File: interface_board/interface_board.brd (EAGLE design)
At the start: 65 x 56 mm, 91 parts, among them IC1 V7805-1000, IC6 LAN9512-JZX, K2 61400826021, Q1 IRLML6346TRPBF, Q6 FA-238 25.0000MB, U1 AL5812MP-13, U2 MPU-9250

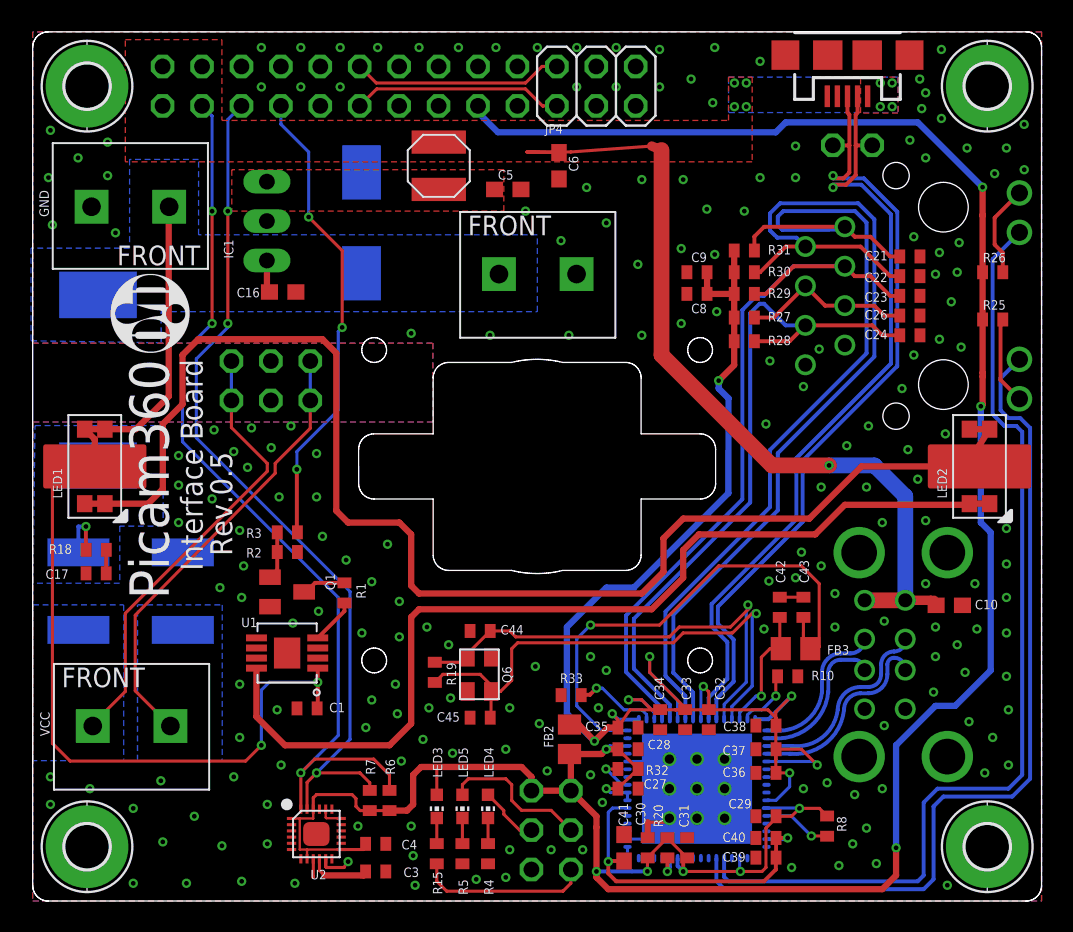
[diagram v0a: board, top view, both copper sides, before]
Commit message: camera_unit, camera_adapter
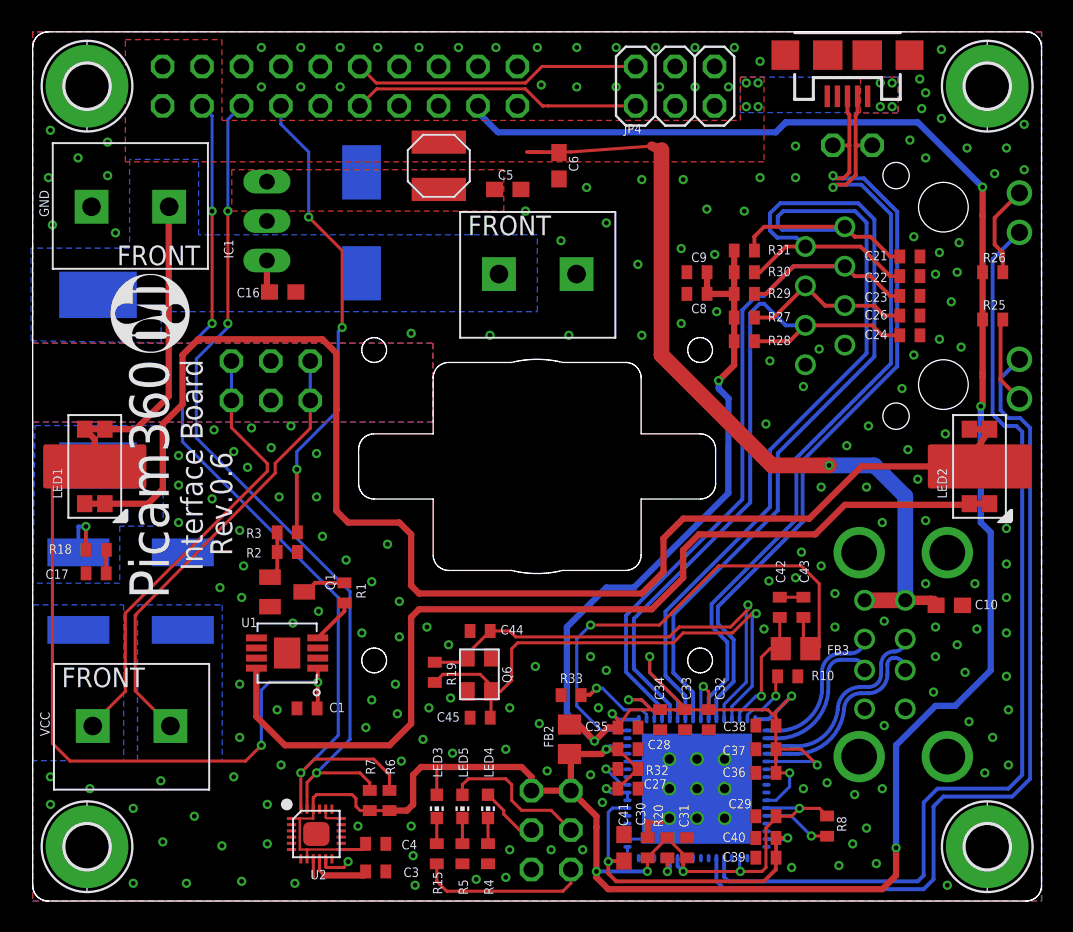
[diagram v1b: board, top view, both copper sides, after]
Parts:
- moved JP4 5.08 mm to (41.4, 52.5)
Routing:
- net PWMA: track 13.6 -> 18.7 mm
- net PWMB: track 13.6 -> 18.7 mm
- net GND: vias 205 -> 207
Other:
- board text added: "Rev.0.6"
- board text removed: "Rev.0.5"
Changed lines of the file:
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@@
 <text x="6.23" y="34.901" size="2.54" layer="21" rot="R270">Picam360</text>
 <text x="9.532" y="34.901" size="1.4224" layer="21" rot="R270">Interface Board</text>
-<text x="11.437" y="28.932" size="1.4224" layer="21" rot="R270">Rev.0.5</text>
+<text x="11.437" y="28.932" size="1.4224" layer="21" rot="R270">Rev.0.6</text>
 <text x="0.484" y="12.185" size="0.6096" layer="21" rot="R270">VCC</text>
 <wire x1="0.9372" y1="55.99801875" x2="0.8747" y2="55.992109375" width="0.001" layer="20"/>
@@
 <attribute name="PROD_ID" value="CONN-09505" x="52.495" y="54.5" size="1.778" layer="27" rot="R180" display="off"/>
 </element>
-<element name="JP4" library="pinhead" package="2X03" value="M20-9980345" x="36.31" y="52.5" smashed="yes">
-<attribute name="NAME" x="33.008" y="49.452" size="0.6096" layer="25" ratio="10"/>
-<attribute name="VALUE" x="32.5" y="48.055" size="1.27" layer="27" display="off"/>
+<element name="JP4" library="pinhead" package="2X03" value="M20-9980345" x="41.39" y="52.5" smashed="yes">
+<attribute name="NAME" x="38.088" y="49.452" size="0.6096" layer="25" ratio="10"/>
+<attribute name="VALUE" x="37.58" y="48.055" size="1.27" layer="27" display="off"/>
 </element>
 <element name="LED3" library="led" package="CHIP-LED0603" value="GREEN" x="26.035" y="6.096" smashed="yes" rot="R180">
@@
 <via x="11.684" y="30.353" extent="1-16" drill="0.3"/>
 <via x="18.288" y="26.035" extent="1-16" drill="0.3"/>
-<via x="43.942" y="54.991" extent="1-16" drill="0.3"/>
+<via x="42.672" y="54.991" extent="1-16" drill="0.3"/>
 <via x="24.384" y="36.576" extent="1-16" drill="0.3"/>
 <via x="34.544" y="36.449" extent="1-16" drill="0.3"/>
-<via x="42.418" y="52.959" extent="1-16" drill="0.3"/>
+<via x="42.672" y="52.451" extent="1-16" drill="0.3"/>
 <via x="17.272" y="54.991" extent="1-16" drill="0.3"/>
 <via x="17.272" y="52.451" extent="1-16" drill="0.3"/>
@@
 <via x="63.881" y="47.117" extent="1-16" drill="0.3"/>
 <via x="62.738" y="48.514" extent="1-16" drill="0.3"/>
-<via x="40.386" y="54.864" extent="1-16" drill="0.3"/>
+<via x="40.132" y="54.991" extent="1-16" drill="0.3"/>
 <via x="58.547" y="54.864" extent="1-16" drill="0.3"/>
 <via x="57.15" y="52.959" extent="1-16" drill="0.3"/>
@@
 <via x="56.515" y="49.022" extent="1-16" drill="0.3"/>
 <via x="37.592" y="52.451" extent="1-16" drill="0.3"/>
-<via x="43.815" y="51.435" extent="1-16" drill="0.3"/>
 <via x="4.826" y="48.895" extent="1-16" drill="0.3"/>
 <via x="1.143" y="49.657" extent="1-16" drill="0.3"/>
@@
 <contactref element="C5" pad="2"/>
 <contactref element="C6" pad="2"/>
+<via x="45.212" y="54.991" extent="1-16" drill="0.3"/>
+<via x="32.766" y="52.578" extent="1-16" drill="0.3"/>
+<via x="44.831" y="52.451" extent="1-16" drill="0.3"/>
 </signal>
 <signal name="N$5">
@@
 <vertex x="12.192" y="55.499"/>
 <vertex x="12.192" y="50.292"/>
-<vertex x="44.831" y="50.292"/>
-<vertex x="44.831" y="53.086"/>
-<vertex x="46.355" y="53.086"/>
-<vertex x="46.355" y="47.625"/>
+<vertex x="45.593" y="50.292"/>
+<vertex x="45.593" y="53.086"/>
+<vertex x="47.117" y="53.086"/>
+<vertex x="47.117" y="47.625"/>
 <vertex x="5.969" y="47.625"/>
 </polygon>
@@
 <wire x1="56.218" y1="26.078" x2="56.218" y2="19.375" width="1.016" layer="16"/>
 <polygon width="0.2" layer="16">
-<vertex x="44.831" y="53.086"/>
+<vertex x="45.593" y="53.086"/>
 <vertex x="55.753" y="53.086"/>
 <vertex x="55.753" y="50.8"/>
-<vertex x="44.831" y="50.8"/>
+<vertex x="45.593" y="50.8"/>
 </polygon>
 <via x="55.372" y="51.181" extent="1-16" drill="0.3"/>
@@
 <via x="54.61" y="51.181" extent="1-16" drill="0.3"/>
 <via x="54.61" y="52.705" extent="1-16" drill="0.3"/>
-<via x="45.212" y="51.181" extent="1-16" drill="0.3"/>
 <via x="45.974" y="51.181" extent="1-16" drill="0.3"/>
-<via x="45.212" y="52.705" extent="1-16" drill="0.3"/>
+<via x="46.736" y="51.181" extent="1-16" drill="0.3"/>
 <via x="45.974" y="52.705" extent="1-16" drill="0.3"/>
+<via x="46.736" y="52.705" extent="1-16" drill="0.3"/>
 <polygon width="0.2" layer="1">
 <vertex x="53.34" y="53.086"/>
@@
 <wire x1="32.844" y1="51.228" x2="32.892" y2="51.228" width="0.2" layer="1"/>
 <wire x1="32.892" y1="51.228" x2="33.217" y2="51.23" width="0.2" layer="1"/>
-<wire x1="33.217" y1="51.23" x2="33.77" y2="51.23" width="0.2" layer="1"/>
+<wire x1="33.217" y1="51.23" x2="38.85" y2="51.23" width="0.2" layer="1"/>
 </signal>
 <signal name="PWMB">
@@
 <wire x1="31.75" y1="52.705" x2="32.817" y2="53.772" width="0.2" layer="1"/>
 <wire x1="32.817" y1="53.772" x2="33.704" y2="53.77" width="0.2" layer="1"/>
-<wire x1="33.704" y1="53.77" x2="33.77" y2="53.77" width="0.2" layer="1"/>
+<wire x1="33.704" y1="53.77" x2="38.85" y2="53.77" width="0.2" layer="1"/>
 </signal>
 <signal name="USBD3_P" class="3">

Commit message: interface board 0.7 rpcm board 0.10
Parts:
- removed JP5: (no value), openblw:1X02
- removed U$8: 282836-2, openblw:282836-2
- added C11, C7: 4.7n, resistor:C0402
- added R11, R9: 1M, resistor:R0402
- K2: device Wuerth_Elektronik_eiCan_Communication_Connectors_v2.2:61400826021 -> openblw:61400826021
- moved LOGO1 28.7 mm to (36.0, 42.4), turned to 0 degrees
- moved C39 28.4 mm to (31.4, 26.4), turned to 270 degrees
- moved C41 25.6 mm to (26.8, 26.4)
- moved C30 25.5 mm to (28.4, 26.3)
- moved R20 23.2 mm to (25.9, 21.1), turned to 180 degrees
- moved C31 23.1 mm to (25.9, 19.9), turned to 0 degrees
- moved R8 21.5 mm to (30.8, 11.6), turned to 90 degrees
- moved FB2 20.0 mm to (39.1, 30.0), turned to 90 degrees
- moved C27 19.9 mm to (32.7, 26.4), turned to 90 degrees
- moved C6 19.6 mm to (14.4, 48.9), turned to 180 degrees
- moved C40 19.1 mm to (29.7, 11.6), turned to 90 degrees
- moved R32 18.4 mm to (33.9, 26.4), turned to 90 degrees
- moved FB3 18.3 mm to (37.1, 30.0), turned to 90 degrees
- moved C28 16.8 mm to (35.7, 26.4), turned to 90 degrees
- moved C29 16.4 mm to (32.0, 11.6), turned to 270 degrees
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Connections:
- net N$43 renamed AVDD18PLL
- new net PWMC: JP1.14, JP4.3
- new net PWMD: JP1.15, JP4.5
- new net USB1_SHELL: C7.1, K2.5, K2.6, K2.7, K2.8, R9.1
- new net USB2_SHELL: C11.1, JP6.MT1, JP6.MT2, JP6.P$1, JP6.P$2, R11.1
- net +12V: no longer U$8.CON1
- net +3V3: now also JP1.2
- net GND: now also C11.2, C7.2, R11.2, R9.2; no longer U$8.CON2
- net USB_D_N: no longer JP5.2
- net USB_D_P: no longer JP5.1
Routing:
- net +3V3: track 183.3 -> 31.2 mm, vias 10 -> 17
- net +5V: track 55.3 -> 6.11 mm, vias 9 -> 5
- net VDD18PLL: track 33.3 -> 6.33 mm
- net XI: track 34.5 -> 11.9 mm
- net PWMD: track 0.00 -> 19.7 mm
- net PWMC: track 0.00 -> 19.5 mm
- net XO: track 30.6 -> 11.2 mm
- net NSPD_LED: track 56.4 -> 74.4 mm
- net NLNKA_LED: track 63.0 -> 80.6 mm
- net N$1: track 89.6 -> 73.2 mm
- net USBD3_N: track 12.0 -> 27.3 mm
- net USBD3_P: track 12.1 -> 26.8 mm
- net AVDD18PLL: track 8.34 -> 23.0 mm, vias 1 -> 2
- net 3V3A: track 98.0 -> 83.5 mm, vias 9 -> 14
- net USBD2_P: track 9.27 -> 22.4 mm
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- added copper zone on layer 2, net +3V3
- added copper zone on layer 2, net +5V
- added copper zone on layer 15, net GND
- added copper zone on layer 1, net USB1_SHELL
- added copper zone on layer 1, net USB2_SHELL
- removed copper zone on layer 16, net +5V
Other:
- outline, holes or cut-outs redrawn
- board text added: "Rev.0.7"
- board text removed: "Rev.0.6"

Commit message: after test
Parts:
- moved C8 0.70 mm to (42.0, 38.4)
- moved R29 0.70 mm to (45.8, 38.4)
- moved R27 0.70 mm to (45.8, 36.9)
- moved R28 0.70 mm to (45.8, 35.4)
- moved C9 0.60 mm to (42.0, 39.9)
- moved R9 0.10 mm to (59.1, 16.9)
- moved R7 0.10 mm to (21.7, 6.68)
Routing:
- net RX_P: track 39.5 -> 40.2 mm

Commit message: interface board
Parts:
- moved C1 1.09 mm to (22.0, 16.6), turned to 90 degrees
- moved C40 0.30 mm to (29.4, 11.6)
- moved R8 0.20 mm to (30.6, 11.6)
- moved C29 0.10 mm to (31.9, 11.6)
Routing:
- net +12V: track 72.7 -> 75.5 mm

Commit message: revert to 2.7mm hole for camera
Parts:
- moved C1 1.09 mm to (20.9, 16.8), turned to 180 degrees
- moved C40 0.30 mm to (29.7, 11.6)
- moved R8 0.20 mm to (30.8, 11.6)
- moved C29 0.10 mm to (32.0, 11.6)
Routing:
- net +12V: track 75.5 -> 72.7 mm
